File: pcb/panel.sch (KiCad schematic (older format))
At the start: 19 parts, among them IC1 ATMEGA88P-20PU, P1 SERIAL, P2 I2C, P3 KEYBOARD, P4 CONN_1, P5 CONN_1, P6 CONN_1, P7 CONN_1, U1 2X16DIGIT-DISPLAY

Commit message: some improvements on panel.sch
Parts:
- removed P4, P5, P6, P7: CONN_1, symbol CONN_1
- renumbered BC547C1 to BC1, P1 to P5, P2 to P6, P3 to P7, R2 to R1, R1 to R2, 100nF1 to U2, 100uF1 to U3
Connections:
- wire segments 76 -> 71
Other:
- moved on the sheet: BC1, D1, D2, F1, IC1, P5, P6, P7, R1, R2, R3, RV1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

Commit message: moved some more pins around!
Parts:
- removed D2: LED, symbol LED
- removed R3: 330, symbol R
- added D?: LED, symbol LED
- added R?: 330, symbol R
- R1: value R -> 330
- renumbered P5 to P1, P6 to P2, P7 to P3
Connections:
- net +5V: now also D?.1 (A)
- net GND: no longer F1.2 (PM), IC1.8 (GND)
- net at IC1.15 (PB1_(OC1A/PCINT1)): now also P3.3 (P3)
- net at IC1.16 (PB2_(SS/OC1B/PCINT2)): now also P3.4 (P4); no longer P3.7 (P7)
- net at IC1.17 (PB3_(MOSI/OC2A/PCINT3)): now also P3.5 (P5); no longer P3.6 (P6)
- net at IC1.18 (PB4_(MISO/PCINT4)): now also P3.6 (P6); no longer P3.5 (P5)
- net at IC1.19 (PB5_(SCK/PCINT5)): now also P3.7 (P7); no longer P3.4 (P4)
- net at IC1.23 (PC0_(ADC0/PCINT8)): now also P3.1 (P1); no longer P3.3 (P3)
- net at IC1.25 (PC2_(ADC2/PCINT10)): now also R2.1; no longer P3.1 (P1)
- net at IC1.26 (PC3_(ADC3/PCINT11)): now also R?.2; no longer R2.1
- net at IC1.4 (2): now also U1.4 (RS); no longer R1.1
- net at IC1.5 (3): now also U1.6 (E); no longer U1.4 (RS)
- net at IC1.6 (4): now also R1.1; no longer U1.6 (E)
- new net: F1.2 (PM), IC1.8 (GND)
- new net: D?.2 (K), R?.1
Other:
- moved on the sheet: D1, F1, P3, R1
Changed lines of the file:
@@
-EESchema Schematic File Version 2  date Sat 02 Jul 2011 11:04:16 AM CEST
+EESchema Schematic File Version 2  date Sat 02 Jul 2011 08:58:42 PM CEST
 LIBS:panel-cache
 LIBS:power
@@
 $EndDescr
 Wire Wire Line
-	3300 2200 1550 2200
-Wire Wire Line
-	5300 2500 6000 2500
+	1750 2250 2150 2250
+Wire Wire Line
+	1750 2250 1750 2350
+Wire Wire Line
+	5850 1900 5950 1900
+Wire Wire Line
+	7750 3400 7750 2000
+Connection ~ 2400 2300
+Wire Wire Line
+	2400 2200 2400 2300
+Wire Wire Line
+	1550 2000 3300 2000
+Wire Wire Line
+	5300 2200 7400 2200
+Wire Wire Line
+	7400 2200 7400 3300
+Wire Wire Line
+	7400 3300 6850 3300
+Wire Wire Line
+	6850 3300 6850 3200
+Wire Wire Line
+	6000 2500 5300 2500
 Wire Wire Line
 	2050 3400 4050 3400
 Wire Wire Line
-	3300 2400 3050 2400
+	3300 2400 2150 2400
 Wire Wire Line
 	2900 1100 2900 1350
 Wire Wire Line
-	3300 2100 2100 2100
-Wire Wire Line
-	2100 2100 2100 2000
-Wire Wire Line
-	2100 2000 1550 2000
-Wire Wire Line
 	5800 1600 5500 1600
 Wire Wire Line
 	5500 1600 5500 1200
-Wire Wire Line
-	3100 2000 3300 2000
-Wire Wire Line
-	2600 1950 2600 2000
-Wire Wire Line
-	5850 3000 5300 3000
-Wire Wire Line
-	6950 3000 6850 3000
-Wire Wire Line
-	5300 2200 6500 2200
-Wire Wire Line
-	6500 2200 6500 2500
-Wire Wire Line
-	6500 2500 6850 2500
-Wire Wire Line
-	5300 2000 6700 2000
-Wire Wire Line
-	6700 2000 6700 2300
-Wire Wire Line
-	6700 2300 6850 2300
 Wire Wire Line
 	6850 2700 5300 2700
@@
 	3300 1700 3300 1100
 Wire Wire Line
-	3200 2500 3300 2500
+	2400 2500 3300 2500
 Wire Wire Line
 	4000 650  4000 700
@@
 	2900 2500 2900 2500
 Wire Wire Line
-	2650 2250 3050 2250
-Wire Wire Line
-	3050 2250 3050 2400
-Connection ~ 2800 2250
-Wire Wire Line
-	3300 2600 2400 2600
-Wire Wire Line
-	2400 2600 2400 2500
-Wire Wire Line
-	3200 2300 3300 2300
+	2150 2400 2150 2250
+Connection ~ 2000 2250
+Wire Wire Line
+	3300 2600 1600 2600
+Wire Wire Line
+	1600 2600 1600 2500
+Wire Wire Line
+	2350 2300 3300 2300
 Wire Wire Line
 	3300 1800 3100 1800
@@
 Connection ~ 2200 1550
 Wire Wire Line
-	1900 3150 1900 3100
-Wire Wire Line
 	1900 3100 1550 3100
 Wire Wire Line
 	1750 3750 1750 3600
 Wire Wire Line
-	4550 3400 7750 3400
-Wire Wire Line
-	7750 3400 7750 1900
-Wire Wire Line
-	7750 1900 5300 1900
+	7750 3400 4550 3400
 Wire Wire Line
 	5800 1800 5300 1800
@@
 	5300 2600 6850 2600
 Wire Wire Line
-	6850 2400 6600 2400
-Wire Wire Line
-	6600 2400 6600 2100
-Wire Wire Line
-	6600 2100 5300 2100
-Wire Wire Line
 	6000 2300 5300 2300
-Wire Wire Line
-	6450 3000 6350 3000
-Wire Wire Line
-	2600 1550 2600 1450
 Wire Wire Line
 	5300 1700 5800 1700
@@
 	5700 2400 5700 2500
 Connection ~ 5700 2500
-$Comp
-L +5V #PWR01
+Wire Wire Line
+	5300 3000 6850 3000
+Wire Wire Line
+	6850 3100 6750 3100
+Wire Wire Line
+	6750 3100 6750 3350
+Wire Wire Line
+	6750 3350 7500 3350
+Wire Wire Line
+	7500 3350 7500 2100
+Wire Wire Line
+	7500 2100 5300 2100
+Wire Wire Line
+	1550 2200 1850 2200
+Wire Wire Line
+	1850 2200 1850 2100
+Wire Wire Line
+	1850 2100 3300 2100
+Wire Wire Line
+	7750 2000 5300 2000
+Wire Wire Line
+	5300 1900 5350 1900
+Wire Wire Line
+	6350 1900 6450 1900
+$Comp
+L GND #PWR?
+U 1 1 4E0F5994
+P 1750 2300
+F 0 "#PWR?" H 1750 2300 30  0001 C CNN
+F 1 "GND" H 1750 2230 30  0001 C CNN
+	1    1750 2300
+	1    0    0    -1
+$EndComp
+$Comp
+L +5V #PWR?
+U 1 1 4E0F41E3
+P 6450 1900
+F 0 "#PWR?" H 6450 1990 20  0001 C CNN
+F 1 "+5V" H 6450 1990 30  0000 C CNN
+	1    6450 1900
+	0    1    1    0
+$EndComp
+$Comp
+L LED D?
+U 1 1 4E0F41D3
+P 6150 1900
+F 0 "D?" H 6150 2000 50  0000 C CNN
+F 1 "LED" H 6150 1800 50  0000 C CNN
+	1    6150 1900
+	-1   0    0    1
+$EndComp
+$Comp
+L R R?
+U 1 1 4E0F41C9
+P 5600 1900
+F 0 "R?" V 5680 1900 50  0000 C CNN
+F 1 "330" V 5600 1900 50  0000 C CNN
+	1    5600 1900
+	0    1    1    0
+$EndComp
+$Comp
+L +5V #PWR5
 U 1 1 4E0E490F
-P 2600 1450
-F 0 "#PWR01" H 2600 1540 20  0001 C CNN
-F 1 "+5V" H 2600 1540 30  0000 C CNN
-	1    2600 1450
+P 1800 700
+F 0 "#PWR5" H 1800 790 20  0001 C CNN
+F 1 "+5V" H 1800 790 30  0000 C CNN
+	1    1800 700
 	1    0    0    -1
 $EndComp
@@
 L LED D1
 U 1 1 4E0E4902
-P 2600 1750
-F 0 "D1" H 2600 1850 50  0000 C CNN
-F 1 "LED" H 2600 1650 50  0000 C CNN
-	1    2600 1750
-	0    1    1    0
+P 2600 2200
+F 0 "D1" H 2600 2300 50  0000 C CNN
+F 1 "LED" H 2600 2100 50  0000 C CNN
+	1    2600 2200
+	1    0    0    -1
 $EndComp
 $Comp
 L R R1
 U 1 1 4E0E48F8
-P 2850 2000
-F 0 "R1" V 2930 2000 50  0000 C CNN
-F 1 "R" V 2850 2000 50  0000 C CNN
-	1    2850 2000
-	0    1    1    0
-$EndComp
-$Comp
-L +5V #PWR02
-U 1 1 4E0E48BB
-P 6950 3000
-F 0 "#PWR02" H 6950 3090 20  0001 C CNN
-F 1 "+5V" H 6950 3090 30  0000 C CNN
-	1    6950 3000
-	0    1    1    0
-$EndComp
-$Comp
-L LED D2
-U 1 1 4E0E48A7
-P 6650 3000
-F 0 "D2" H 6650 3100 50  0000 C CNN
-F 1 "LED" H 6650 2900 50  0000 C CNN
-	1    6650 3000
-	-1   0    0    1
-$EndComp
-$Comp
-L R R3
-U 1 1 4E0E488E
-P 6100 3000
-F 0 "R3" V 6180 3000 50  0000 C CNN
-F 1 "330" V 6100 3000 50  0000 C CNN
-	1    6100 3000
-	0    1    1    0
-$EndComp
-$Comp
-L +5V #PWR03
+P 3050 2200
+F 0 "R1" V 3130 2200 50  0000 C CNN
+F 1 "330" V 3050 2200 50  0000 C CNN
+	1    3050 2200
+	0    1    1    0
+$EndComp
+$Comp
+L +5V #PWR15
 U 1 1 4E0E4866
 P 6000 2500
-F 0 "#PWR03" H 6000 2590 20  0001 C CNN
+F 0 "#PWR15" H 6000 2590 20  0001 C CNN
 F 1 "+5V" H 6000 2590 30  0000 C CNN
 	1    6000 2500
@@
 $EndComp
 $Comp
-L GND #PWR04
+L GND #PWR14
 U 1 1 4E0E484A
 P 6000 2300
-F 0 "#PWR04" H 6000 2300 30  0001 C CNN
+F 0 "#PWR14" H 6000 2300 30  0001 C CNN
 F 1 "GND" H 6000 2230 30  0001 C CNN
 	1    6000 2300
@@
 $EndComp
 $Comp
-L GND #PWR05
+L GND #PWR12
 U 1 1 4E0E47C5
 P 5500 1200
-F 0 "#PWR05" H 5500 1200 30  0001 C CNN
+F 0 "#PWR12" H 5500 1200 30  0001 C CNN
 F 1 "GND" H 5500 1130 30  0001 C CNN
 	1    5500 1200
@@
 $EndComp
 $Comp
-L +5V #PWR06
+L +5V #PWR13
 U 1 1 4E0E47C0
 P 5600 1250
-F 0 "#PWR06" H 5600 1340 20  0001 C CNN
+F 0 "#PWR13" H 5600 1340 20  0001 C CNN
 F 1 "+5V" H 5600 1340 30  0000 C CNN
 	1    5600 1250
@@
 $EndComp
 $Comp
-L GND #PWR07
+L GND #PWR2
 U 1 1 4E0E4728
 P 1750 3750
-F 0 "#PWR07" H 1750 3750 30  0001 C CNN
+F 0 "#PWR2" H 1750 3750 30  0001 C CNN
 F 1 "GND" H 1750 3680 30  0001 C CNN
 	1    1750 3750
@@
 $EndComp
 $Comp
-L +5V #PWR08
+L +5V #PWR3
 U 1 1 4E0E4684
 P 1900 3100
-F 0 "#PWR08" H 1900 3190 20  0001 C CNN
+F 0 "#PWR3" H 1900 3190 20  0001 C CNN
 F 1 "+5V" H 1900 3190 30  0000 C CNN
 	1    1900 3100
@@
 $EndComp
 $Comp
-L +5V #PWR09
+L +5V #PWR4
 U 1 1 4E0E4596
 P 2200 1400
-F 0 "#PWR09" H 2200 1490 20  0001 C CNN
+F 0 "#PWR4" H 2200 1490 20  0001 C CNN
 F 1 "+5V" H 2200 1490 30  0000 C CNN
 	1    2200 1400
@@
 $EndComp
 $Comp
-L GND #PWR010
+L GND #PWR1
 U 1 1 4E0E4574
 P 1700 1400
-F 0 "#PWR010" H 1700 1400 30  0001 C CNN
+F 0 "#PWR1" H 1700 1400 30  0001 C CNN
 F 1 "GND" H 1700 1330 30  0001 C CNN
 	1    1700 1400
@@
 $EndComp
 $Comp
-L +5V #PWR011
+L +5V #PWR9
 U 1 1 4E0E43D1
-P 3200 2300
-F 0 "#PWR011" H 3200 2390 20  0001 C CNN
-F 1 "+5V" H 3200 2390 30  0000 C CNN
-	1    3200 2300
+P 2350 2300
+F 0 "#PWR9" H 2350 2390 20  0001 C CNN
+F 1 "+5V" H 2350 2390 30  0000 C CNN
+	1    2350 2300
 	0    -1   -1   0
 $EndComp
@@
 L CERAMIC_FILTER F1
 U 1 1 4E0E42A2
-P 2800 2450
-F 0 "F1" H 2850 2600 50  0000 C CNN
-F 1 "CERAMIC_FILTER" H 2850 2350 40  0000 L CNN
-	1    2800 2450
-	-1   0    0    1
-$EndComp
-$Comp
-L GND #PWR012
+P 2000 2450
+F 0 "F1" H 2050 2600 50  0000 C CNN
+F 1 "CERAMIC_FILTER" H 2050 2350 40  0000 L CNN
+	1    2000 2450
+	-1   0    0    1
+$EndComp
+$Comp
+L GND #PWR6
 U 1 1 4E0E42C0
 P 2650 2250
-F 0 "#PWR012" H 2650 2250 30  0001 C CNN
+F 0 "#PWR6" H 2650 2250 30  0001 C CNN
 F 1 "GND" H 2650 2180 30  0001 C CNN
 	1    2650 2250
@@
 $EndComp
 $Comp
-L +5V #PWR013
+L +5V #PWR10
 U 1 1 4E0E4202
 P 4000 650
-F 0 "#PWR013" H 4000 740 20  0001 C CNN
+F 0 "#PWR10" H 4000 740 20  0001 C CNN
 F 1 "+5V" H 4000 740 30  0000 C CNN
 	1    4000 650
@@
 $EndComp
 $Comp
-L GND #PWR014
+L GND #PWR11
 U 1 1 4E0E41FB
 P 4000 1150
-F 0 "#PWR014" H 4000 1150 30  0001 C CNN
+F 0 "#PWR11" H 4000 1150 30  0001 C CNN
 F 1 "GND" H 4000 1080 30  0001 C CNN
 	1    4000 1150
@@
 $EndComp
 $Comp
-L GND #PWR015
+L GND #PWR8
 U 1 1 4E0E41BD
 P 3200 1400
-F 0 "#PWR015" H 3200 1400 30  0001 C CNN
+F 0 "#PWR8" H 3200 1400 30  0001 C CNN
 F 1 "GND" H 3200 1330 30  0001 C CNN
 	1    3200 1400
@@
 $EndComp
 $Comp
-L +5V #PWR016
+L +5V #PWR7
 U 1 1 4E0E41A5
 P 2900 1350
-F 0 "#PWR016" H 2900 1440 20  0001 C CNN
+F 0 "#PWR7" H 2900 1440 20  0001 C CNN
 F 1 "+5V" H 2900 1440 30  0000 C CNN
 	1    2900 1350
@@
 $EndComp
 $Comp
-L CONN_5 P5
+L CONN_5 P1
 U 1 1 4E0E4171
 P 3100 700
-F 0 "P5" V 3050 700 50  0000 C CNN
+F 0 "P1" V 3050 700 50  0000 C CNN
 F 1 "SERIAL" V 3150 700 50  0000 C CNN
 	1    3100 700
@@
 $EndComp
 $Comp
-L CONN_7 P7
+L CONN_7 P3
 U 1 1 4E0E2642
-P 7200 2600
-F 0 "P7" V 7170 2600 60  0000 C CNN
-F 1 "KEYBOARD" V 7270 2600 60  0000 C CNN
-	1    7200 2600
-	1    0    0    -1
-$EndComp
-$Comp
-L CONN_4 P6
+P 7200 2900
+F 0 "P3" V 7170 2900 60  0000 C CNN
+F 1 "KEYBOARD" V 7270 2900 60  0000 C CNN
+	1    7200 2900
+	1    0    0    1
+$EndComp
+$Comp
+L CONN_4 P2
 U 1 1 4E0E25F8
 P 6150 1650
-F 0 "P6" V 6100 1650 50  0000 C CNN
+F 0 "P2" V 6100 1650 50  0000 C CNN
 F 1 "I2C" V 6200 1650 50  0000 C CNN
 	1    6150 1650

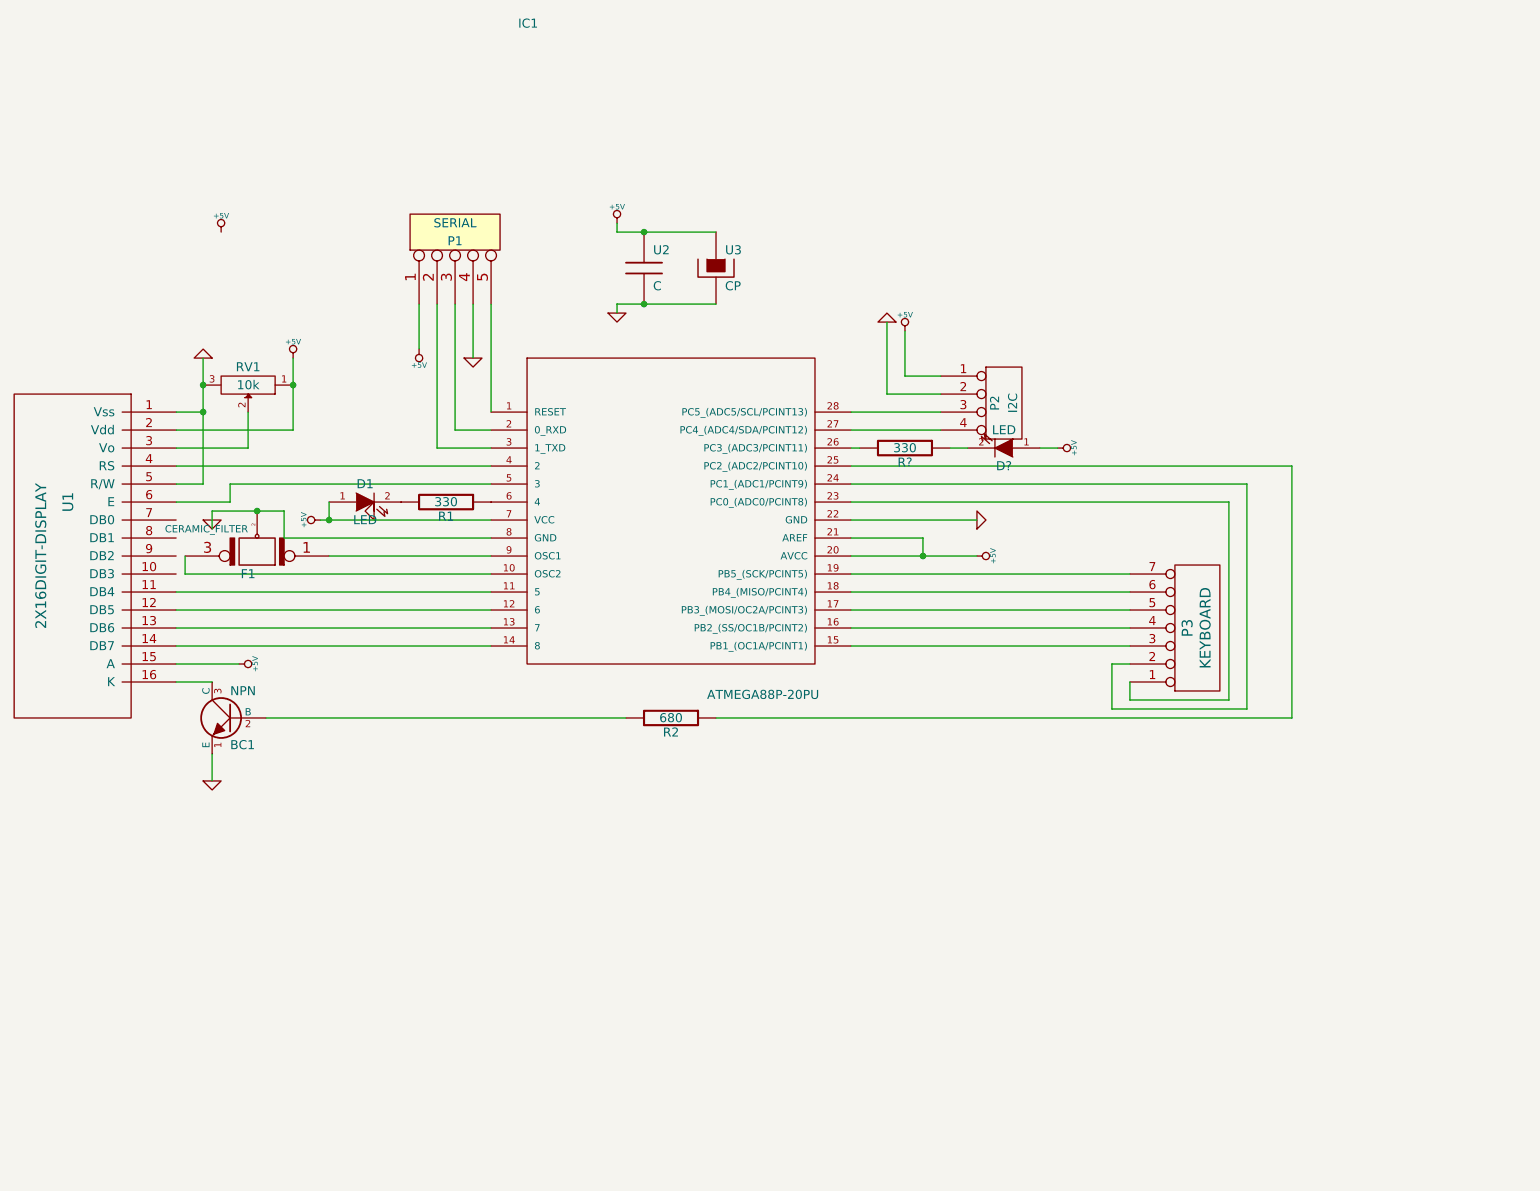
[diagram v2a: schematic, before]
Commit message: Revision 0.2 of the PCB, with firmware for the arduino updated to a hopefully more logical pinout
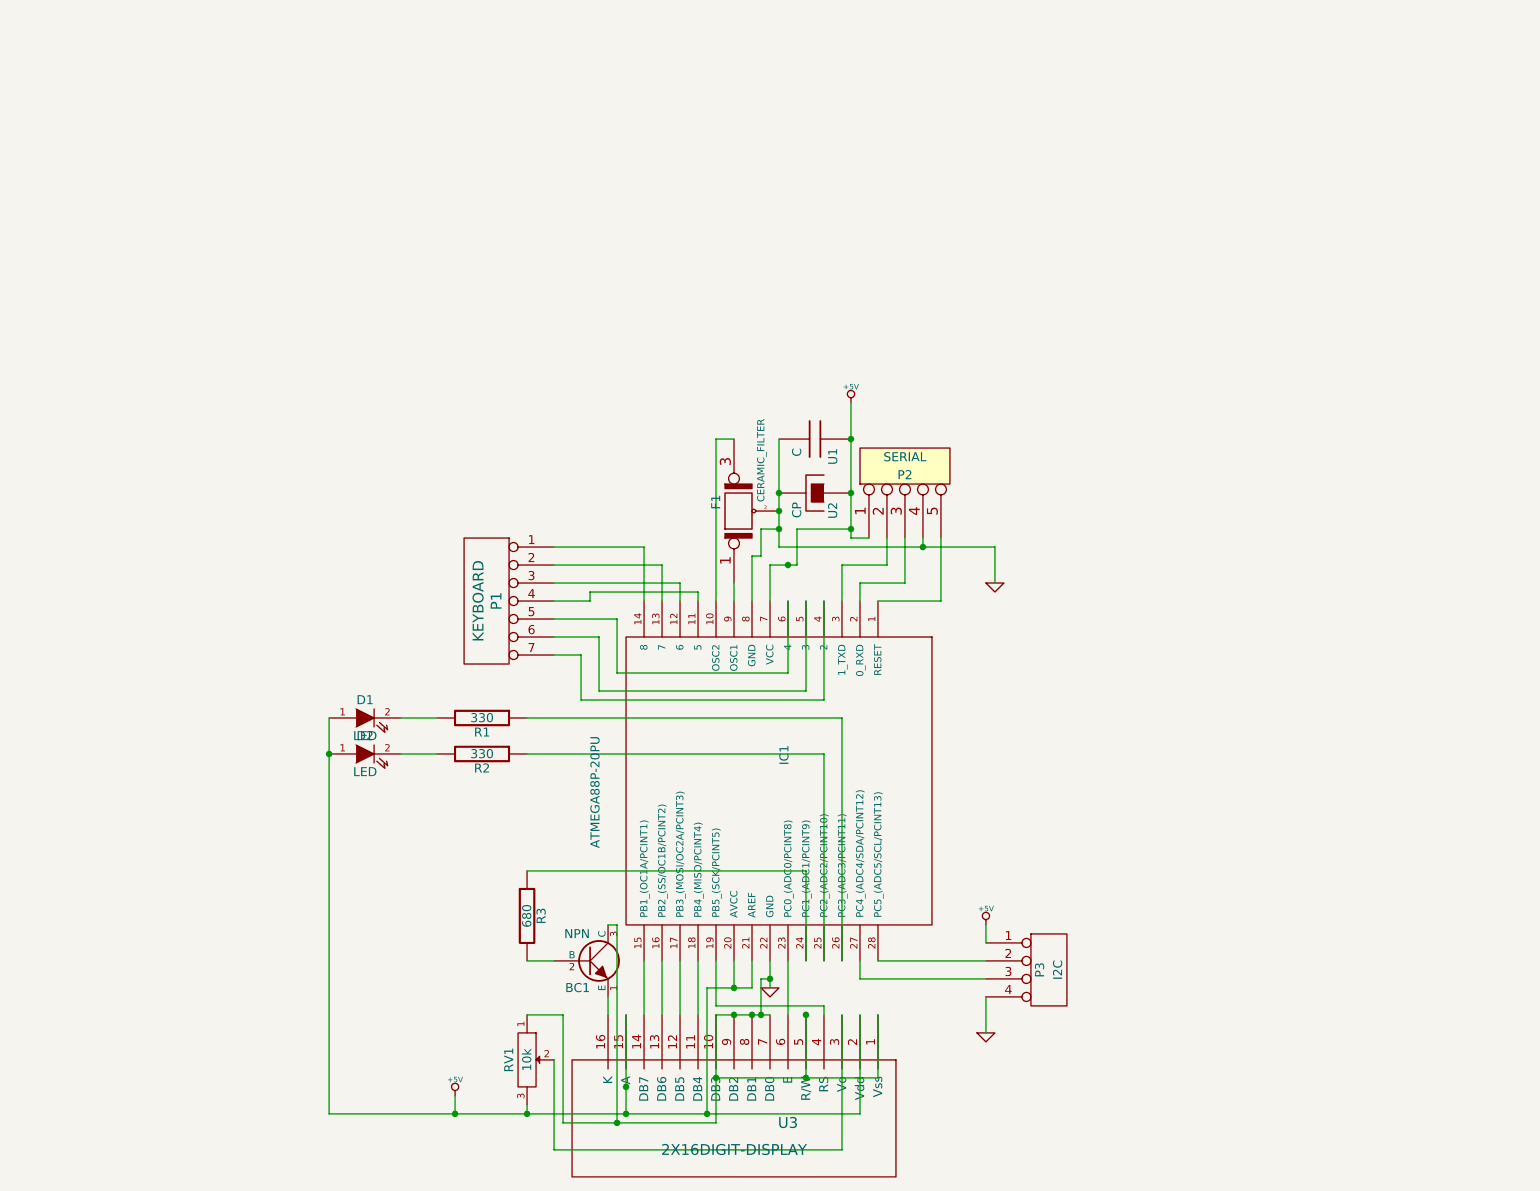
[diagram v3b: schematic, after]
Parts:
- gave numbers to parts that had none: 2
- renumbered P3 to P1, P1 to P2, P2 to P3, R2 to R3, U2 to U1, U3 to U2, U1 to U3
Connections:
- net +5V: now also RV1.3; no longer RV1.1
- net GND: now also BC1.3 (C), F1.2 (PM), IC1.8 (GND), P3.4 (P4), RV1.1, U3.10 (DB3), U3.7 (DB0), U3.8 (DB1), U3.9 (DB2); no longer BC1.1 (E), P3.2 (P2), RV1.3
- net at IC1.11 (5): now also P1.4 (P4); no longer U3.11 (DB4)
- net at IC1.12 (6): now also P1.3 (P3); no longer U3.12 (DB5)
- net at IC1.13 (7): now also P1.2 (P2); no longer U3.13 (DB6)
- net at IC1.14 (8): now also P1.1 (P1); no longer U3.14 (DB7)
- net at IC1.15 (PB1_(OC1A/PCINT1)): now also U3.14 (DB7); no longer P1.3 (P3)
- net at IC1.16 (PB2_(SS/OC1B/PCINT2)): now also U3.13 (DB6); no longer P1.4 (P4)
- net at IC1.17 (PB3_(MOSI/OC2A/PCINT3)): now also U3.12 (DB5); no longer P1.5 (P5)
- net at IC1.18 (PB4_(MISO/PCINT4)): now also U3.11 (DB4); no longer P1.6 (P6)
- net at IC1.19 (PB5_(SCK/PCINT5)): now also U3.4 (RS); no longer P1.7 (P7)
- net at IC1.23 (PC0_(ADC0/PCINT8)): now also U3.6 (E); no longer P1.1 (P1)
- net at IC1.24 (PC1_(ADC1/PCINT9)): now also R3.1; no longer P1.2 (P2)
- net at IC1.25 (PC2_(ADC2/PCINT10)): now also R2.1; no longer R3.1
- net at IC1.26 (PC3_(ADC3/PCINT11)): now also R1.1; no longer R2.2
- net at IC1.27 (PC4_(ADC4/SDA/PCINT12)): now also P3.3 (P3); no longer P3.4 (P4)
- net at IC1.28 (PC5_(ADC5/SCL/PCINT13)): now also P3.2 (P2); no longer P3.3 (P3)
- net at IC1.4 (2): now also P1.7 (P7); no longer U3.4 (RS)
- net at IC1.5 (3): now also P1.6 (P6); no longer U3.6 (E)
- net at IC1.6 (4): now also P1.5 (P5); no longer R1.1
- net at U3.16 (K): now also BC1.1 (E); no longer BC1.3 (C)
- net at D2.2 (K): now also R2.2; no longer R2.1
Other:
- moved on the sheet: BC1, D1, D2, F1, IC1, P1, P2, P3, R1, R2, R3, RV1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
